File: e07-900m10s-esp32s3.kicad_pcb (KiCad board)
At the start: 2 copper layers, 66.5 x 63.2 mm, 23 parts, among them J1 Conn_01x08_Pin, J2 C3/S3mini, U1 E07-900M10S, U2 ESP32-S3-DevKitC

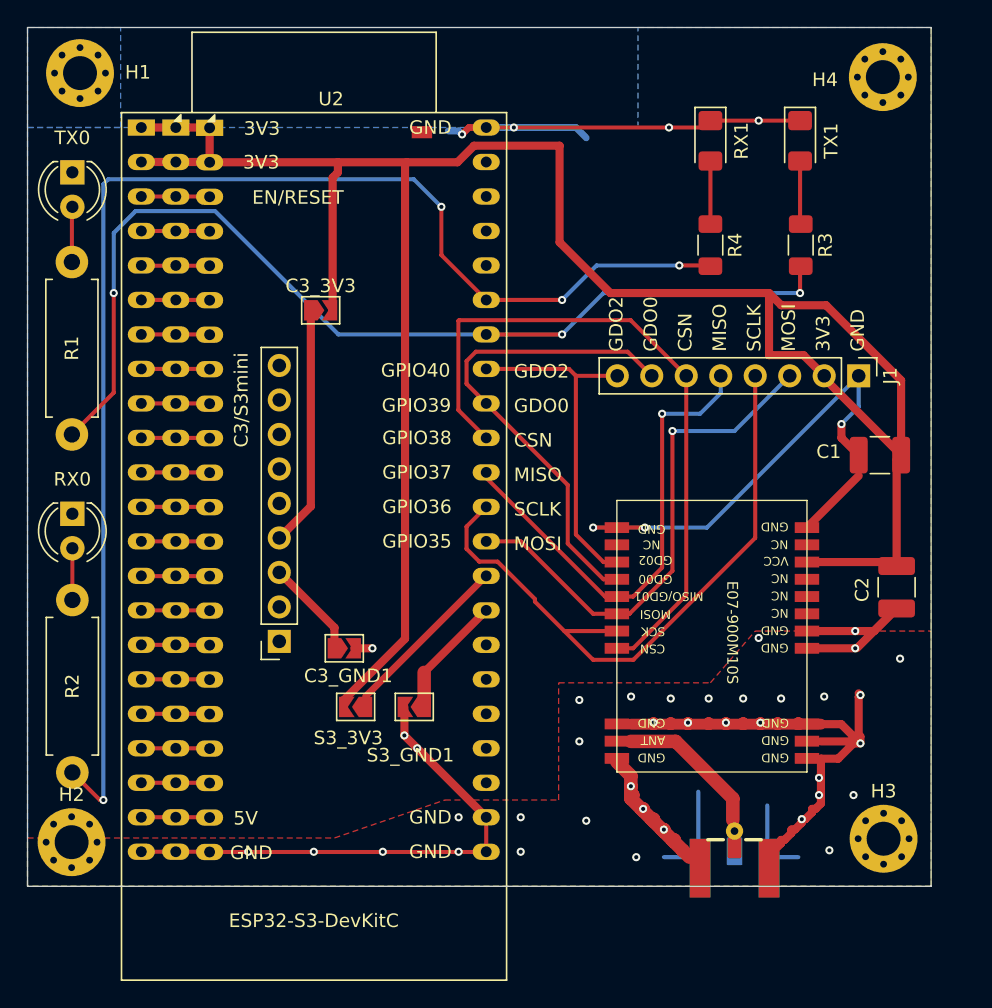
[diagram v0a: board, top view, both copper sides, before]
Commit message: New version for JLC production
Header removed, PCB extended LED's switched for standard basic part and added MPN to components JLC solders.
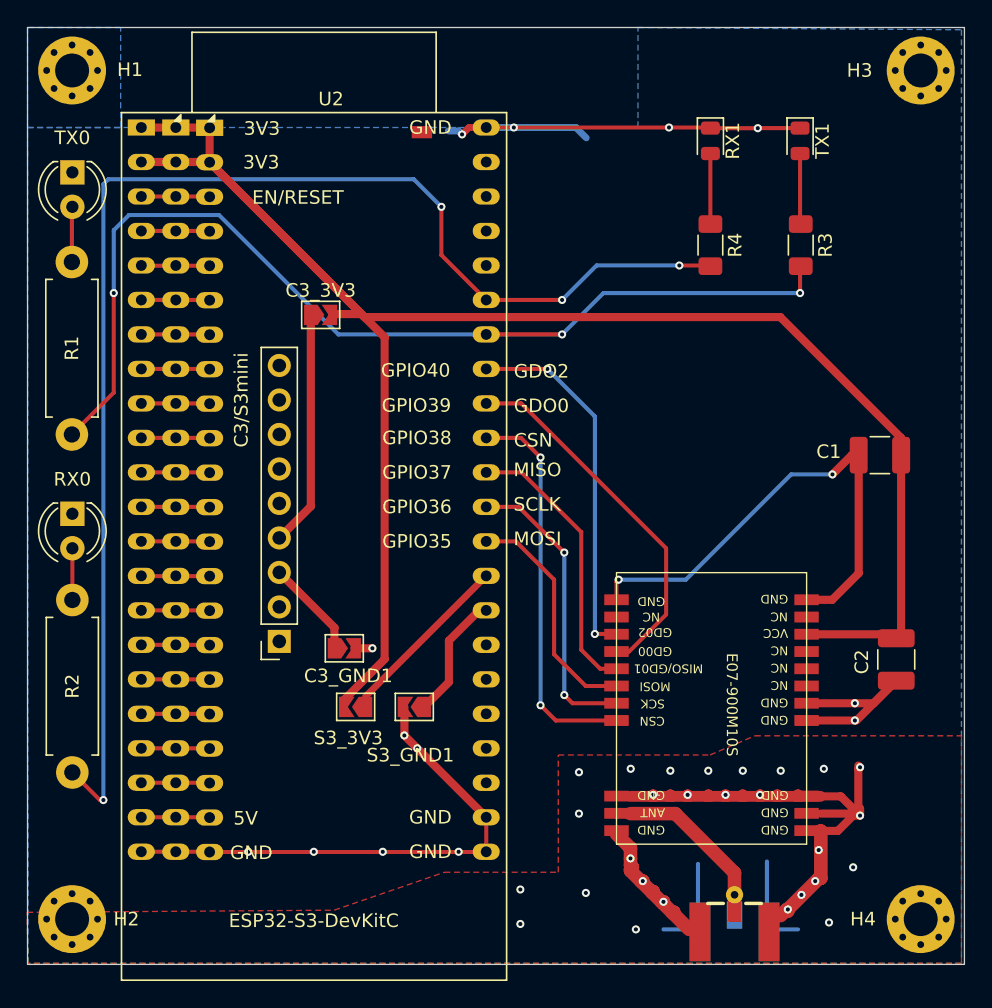
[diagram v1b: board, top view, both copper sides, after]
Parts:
- removed J1: Conn_01x08_Pin, Connector_PinHeader_2.54mm:PinHeader_1x08_P2.54mm_Vertical
- C2: value 4.7uF -> 10uF
- R3, R4: value 220R -> 1000R
- RX1: value LED_RX -> LED_RED; footprint LED_SMD:LED_1206_3216Metric_Pad1.42x1.75mm_HandSolder -> LED_SMD:LED_0805_2012Metric
- TX1: value LED_TX -> LED_BLUE; footprint LED_SMD:LED_1206_3216Metric_Pad1.42x1.75mm_HandSolder -> LED_SMD:LED_0805_2012Metric
- moved H4 62.1 mm to (159.0, 134.5)
- moved H3 56.6 mm to (159.0, 72.0)
- moved H2 5.67 mm to (96.5, 134.5)
- moved C2 5.32 mm to (157.2, 115.4)
- moved U1 5.32 mm to (150.6, 128.0)
- moved J$1 4.69 mm to (145.3, 135.2)
- moved H1 0.61 mm to (96.5, 72.0)
- moved C3_3V3 0.34 mm to (114.8, 90.0)
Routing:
- net /SCLK: track 48.0 -> 21.7 mm, vias 0 -> 2
- net 3V3: track 166.5 -> 141.7 mm
- net /CSN: track 50.9 -> 28.9 mm, vias 0 -> 2
- net /MOSI: track 37.9 -> 17.2 mm, vias 1 -> 0
- net /MISO: track 35.4 -> 20.7 mm, vias 1 -> 0
- net /GDO0: track 35.9 -> 27.3 mm
- net GND: track 194.0 -> 202.2 mm, vias 45 -> 42
- net /GDO2: track 25.4 -> 27.0 mm, vias 0 -> 2
- net unconnected-(U2-GPIO46-Pad14): track 5.80 -> 5.01 mm
- net Net-(RX1-A): track 4.64 -> 5.19 mm
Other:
- board size 66.5 x 63.2 mm -> 69 x 69 mm
- board text removed: "3V3"
- board text removed: "GND"
